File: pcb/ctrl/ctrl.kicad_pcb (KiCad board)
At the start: 2 copper layers, 50 x 50 mm, 10 parts, among them J1 Conn_01x15, J2 Conn_01x15

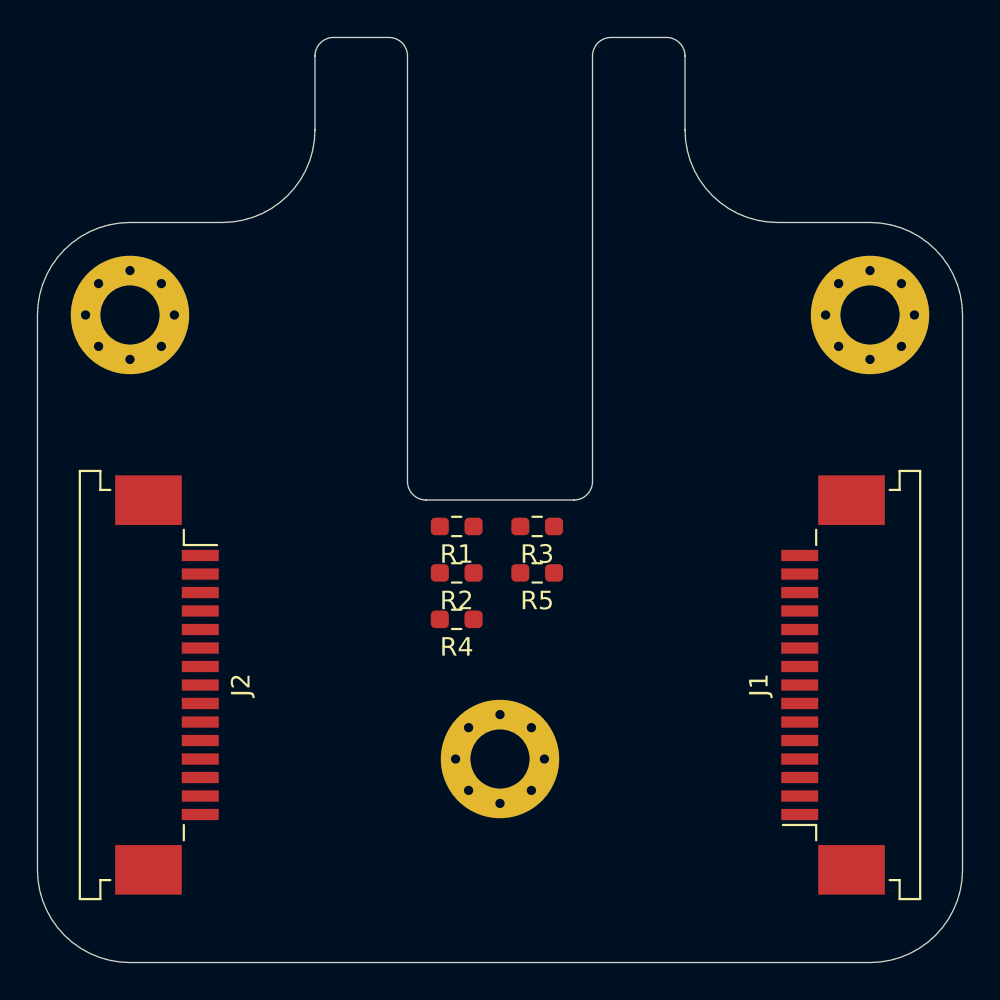
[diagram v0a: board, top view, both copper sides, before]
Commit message: pcb/ctrl Basic schematic and layout, without programming.
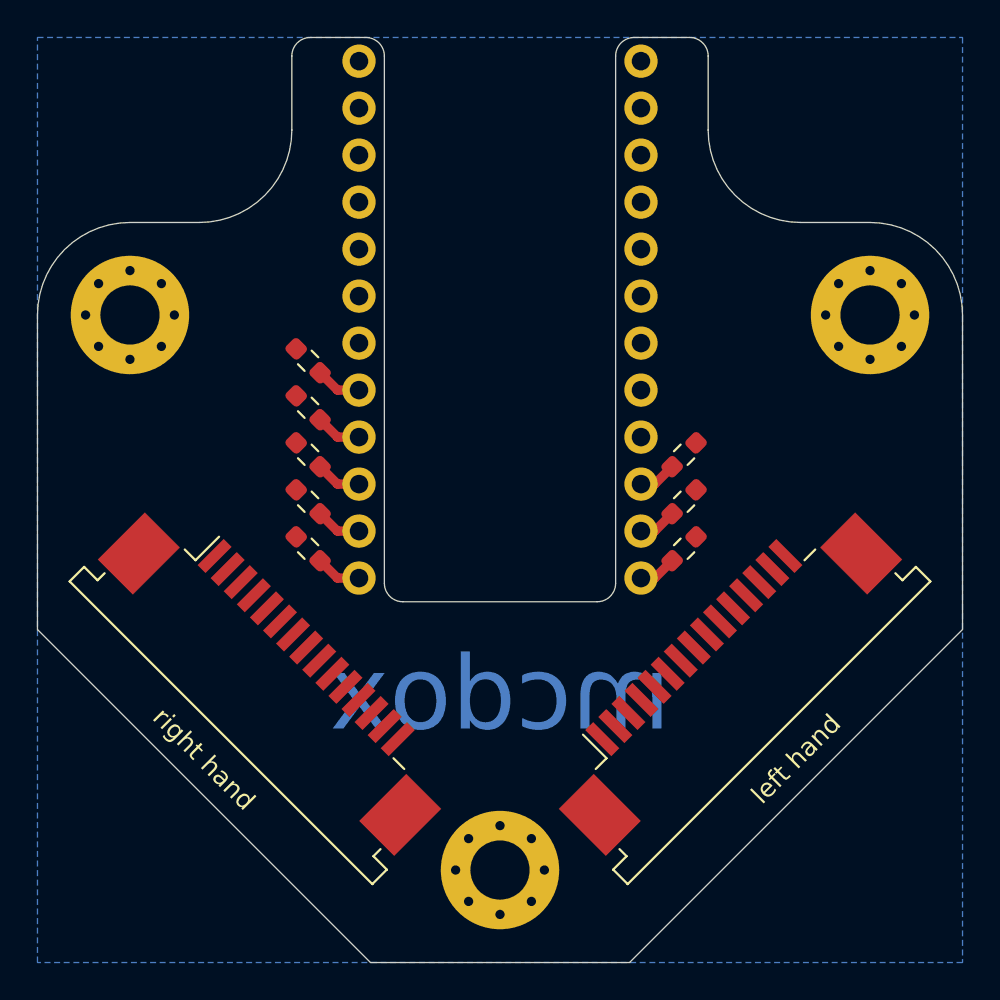
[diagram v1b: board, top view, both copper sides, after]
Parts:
- added R0: 220, ctrl:R_0603_1608Metric_Pad0.98x0.95mm_HandSolder, F.Cu at (234.9, 122.6)
- added R6: 220, ctrl:R_0603_1608Metric_Pad0.98x0.95mm_HandSolder, F.Cu at (214.6, 120.0)
- added R7: 220, ctrl:R_0603_1608Metric_Pad0.98x0.95mm_HandSolder, F.Cu at (214.6, 117.5)
- added U1: ArduinoProMicro, ctrl:ArduinoProMicro, F.Cu at (225.0, 115.2)
- moved Jleft1 29.8 mm to (236.8, 134.2), turned to 45 degrees
- moved Jright1 29.8 mm to (213.2, 134.2), turned to 315 degrees
- moved R5 13.9 mm to (214.6, 122.6), turned to 315 degrees
- moved R3 12.4 mm to (214.6, 127.6), turned to 315 degrees
- moved R1 12.4 mm to (234.9, 125.1), turned to 225 degrees
- moved R2 12.4 mm to (234.9, 127.6), turned to 225 degrees
- moved R4 10.2 mm to (214.6, 125.1), turned to 315 degrees
- moved REF** 6.00 mm to (225.0, 145.0)
- renumbered J2 to Jleft1, J1 to Jright1
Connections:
- Jleft1 pad 1: row0 -> GND
- Jleft1 pad 10: col4 -> col0
- Jleft1 pad 11: col5 -> row5
- Jleft1 pad 12: col6 -> row6
- Jleft1 pad 13: col7 -> row7
- Jleft1 pad 14: Net-(J2-Pad14) -> row8
- Jleft1 pad 15: Net-(J2-Pad15) -> row9
- Jleft1 pad 2: row1 -> +3V3
- Jleft1 pad 3: row2 -> col7
- Jleft1 pad 4: row3 -> col6
- Jleft1 pad 5: row4 -> col5
- Jleft1 pad 6: col0 -> col4
- Jleft1 pad 7: col1 -> col3
- Jleft1 pad 9: col3 -> col1
- Jright1 pad 1: Net-(J1-Pad1) -> row0
- Jright1 pad 10: col0 -> col4
- Jright1 pad 11: row4 -> col5
- Jright1 pad 12: row3 -> col6
- Jright1 pad 13: row2 -> col7
- Jright1 pad 14: row1 -> +3V3
- Jright1 pad 15: row0 -> GND
- Jright1 pad 2: Net-(J1-Pad2) -> row1
- Jright1 pad 3: col7 -> row2
- Jright1 pad 4: col6 -> row3
- Jright1 pad 5: col5 -> row4
- Jright1 pad 6: col4 -> col0
- Jright1 pad 7: col3 -> col1
- Jright1 pad 9: col1 -> col3
- R1 pad 1: Net-(R1-Pad1) -> col1
- R2 pad 1: Net-(R2-Pad1) -> col2
- R3 pad 1: Net-(R3-Pad1) -> col3
- R4 pad 1: Net-(R4-Pad1) -> col4
- R5 pad 1: Net-(R5-Pad1) -> col5
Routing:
- net Net-(R7-Pad2): track 0.00 -> 2.49 mm
- net Net-(R4-Pad2): track 0.00 -> 2.49 mm
- net Net-(R6-Pad2): track 0.00 -> 2.49 mm
- net Net-(R5-Pad2): track 0.00 -> 2.49 mm
- net Net-(R3-Pad2): track 0.00 -> 2.49 mm
- net Net-(R1-Pad2): track 0.00 -> 2.07 mm
- net Net-(R2-Pad2): track 0.00 -> 2.07 mm
- net Net-(R0-Pad2): track 0.00 -> 2.07 mm
- added copper zone on B.Cu, net (none)
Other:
- outline, holes or cut-outs redrawn
- board text added: "Dave McEwan"
- board text added: "Nov 2020"
- board text added: "left hand"
- board text added: "mcdox"
- board text added: "right hand"

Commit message: pcb/ctrl Pushbutton for bootloader programming, and backup ICSP pogo header.
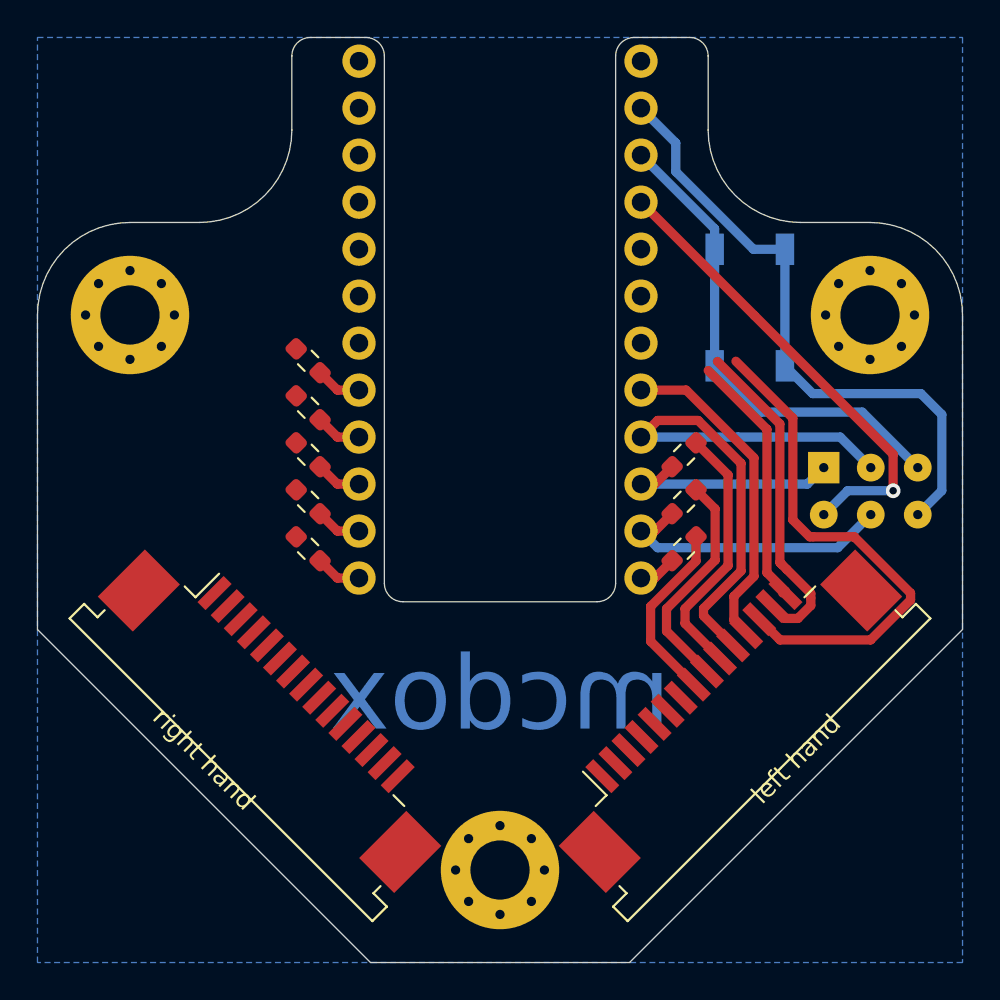
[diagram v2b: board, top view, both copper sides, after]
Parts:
- added Jicsp1: Conn_02x03_Odd_Even, Connector_PinHeader_2.54mm:PinHeader_2x03_P2.54mm_Vertical, B.Cu at (242.5, 123.2)
- added SW1: SW_Push, Button_Switch_SMD:SW_SPST_TL3342, B.Cu at (238.5, 114.6)
- moved Jleft1 2.00 mm to (236.8, 136.2)
- moved Jright1 2.00 mm to (213.2, 136.2)
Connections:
- net +3V3 renamed VCC
- net Net-(R0-Pad2) renamed MISO
- net Net-(R1-Pad2) renamed MOSI
- net row5 renamed SCK
- U1 pad 15: Net-(U1-Pad15) -> RST
- U1 pad 3: Net-(U1-Pad3) -> GND
- U1 pad 4: Net-(U1-Pad4) -> GND
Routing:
- net GND: track 0.00 -> 33.7 mm
- net SCK: track 0.00 -> 31.2 mm
- net row7: track 0.00 -> 27.8 mm
- net RST: track 0.00 -> 26.5 mm
- net VCC: track 0.00 -> 25.7 mm, vias 0 -> 1
- net row8: track 0.00 -> 17.9 mm
- net row6: track 0.00 -> 17.8 mm
- net col0: track 0.00 -> 14.1 mm
- net row9: track 0.00 -> 13.9 mm
- net MOSI: track 2.07 -> 15.6 mm
- net col1: track 0.00 -> 12.2 mm
- net MISO: track 2.07 -> 12.3 mm
- net col2: track 0.00 -> 9.97 mm

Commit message: pdb/ctrl Positions ready for Lolly.
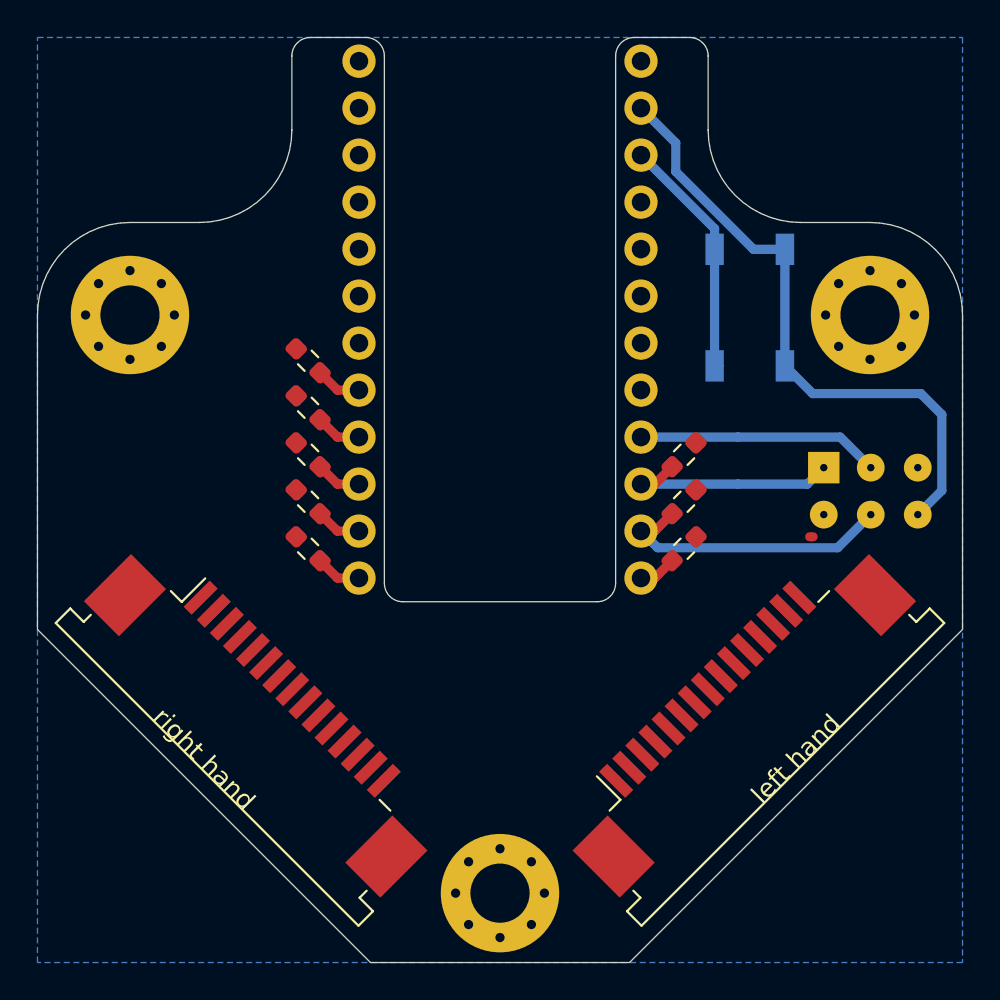
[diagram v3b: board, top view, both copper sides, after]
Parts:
- moved REF** 1.25 mm to (225.0, 146.2)
- moved Jleft1 0.79 mm to (237.5, 136.5)
- moved Jright1 0.79 mm to (212.5, 136.5)
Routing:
- net row7: track 27.8 -> 0.00 mm
- net VCC: track 25.7 -> 0.21 mm, vias 1 -> 0
- net SCK: track 31.2 -> 13.1 mm
- net row8: track 17.9 -> 0.00 mm
- net row6: track 17.8 -> 0.00 mm
- net col0: track 14.1 -> 0.00 mm
- net row9: track 13.9 -> 0.00 mm
- net RST: track 26.5 -> 13.3 mm
- net col1: track 12.2 -> 0.00 mm
- net col2: track 9.97 -> 0.00 mm
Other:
- board text removed: "mcdox"

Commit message: pcb/ctrl Lolly's layout.
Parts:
- SW1: moved to F.Cu
- moved R3 6.54 mm to (219.5, 132.0), turned to 135 degrees
- moved R2 4.92 mm to (233.2, 132.2), turned to 135 degrees
- moved R7 3.58 mm to (215.2, 121.0), turned to 45 degrees
- moved R6 3.54 mm to (215.2, 123.5), turned to 45 degrees
- moved R1 3.52 mm to (234.6, 128.6), turned to 135 degrees
- moved R5 3.50 mm to (215.2, 126.0), turned to 45 degrees
- moved R4 3.46 mm to (215.2, 128.5), turned to 45 degrees
- moved R0 3.41 mm to (234.8, 126.0), turned to 135 degrees
- turned SW1 to 90 degrees
- renumbered Jicsp1 to ICSP
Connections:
- R3 pad 1: col3 -> col7
- R4 pad 1: col4 -> col6
- R6 pad 1: col6 -> col4
- R7 pad 1: col7 -> col3
- U1 pad 3: GND -> Net-(U1-Pad3)
- U1 pad 4: GND -> Net-(U1-Pad4)
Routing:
- net VCC: track 0.21 -> 62.5 mm, vias 0 -> 1
- net col3: track 0.00 -> 51.1 mm, vias 0 -> 2
- net GND: track 33.7 -> 83.3 mm, vias 0 -> 2
- net col4: track 0.00 -> 47.7 mm, vias 0 -> 2
- net col0: track 0.00 -> 45.9 mm, vias 0 -> 2
- net col5: track 0.00 -> 43.7 mm, vias 0 -> 2
- net col1: track 0.00 -> 42.1 mm, vias 0 -> 2
- net col6: track 0.00 -> 41.1 mm, vias 0 -> 2
- net col2: track 0.00 -> 38.2 mm, vias 0 -> 2
- net row1: track 0.00 -> 34.9 mm, vias 0 -> 1
- net col7: track 0.00 -> 34.5 mm, vias 0 -> 2
- net row0: track 0.00 -> 32.5 mm
- net row2: track 0.00 -> 30.6 mm, vias 0 -> 1
- net row3: track 0.00 -> 25.6 mm, vias 0 -> 1
- net row9: track 0.00 -> 23.0 mm
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- added copper zone on F.Cu, net (none)
- added copper zone on B.Cu, net GND
- removed copper zone on B.Cu, net (none)
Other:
- board text added: "GND"
- board text added: "Laid by Lolly"
- board text added: "MISO"
- board text added: "MOSI"
- board text added: "RST"
- board text added: "SCK"
- board text added: "VCC"
- board text added: "lollybrd"
- board text added: "mcdox"
- board text removed: "Dave McEwan"
